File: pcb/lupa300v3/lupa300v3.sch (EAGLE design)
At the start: 17 parts

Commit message: more work
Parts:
- added C1, C2, C3, C4, C5, C6: .1uF, rcl:C-USC0603K
- added JP1, JP2: (no value), pinhead:PINHD-2X8
- added R12, R13, R14, R15, R16, R17, R18, R23: (no value), rcl:R-US_R0603
- added R19: 500k, rcl:R-US_R0603
- added R20: 1.5M, rcl:R-US_R0603
- added R21: 42k, rcl:R-US_R0603
- added R22: 110k, rcl:R-US_R0603
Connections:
- new net ADC_BIAS: C1.1, R12.1, U$1.ADC_BIAS
- new net BIAS1: C2.1, R19.1, U$1.BIAS1
- new net BIAS2: C3.1, R20.1, U$1.BIAS2
- new net BIAS3: C4.1, R21.1, U$1.BIAS3
- new net BIAS4: C5.1, R22.1, U$1.BIAS4
- new net N$27: U$1.VRESET_3
- new net N$28: U$1.VRESET_2
- new net N$29: U$2.GND
- new net N$30: U$2.VIN
- new net N$58: JP1.1
- new net N$59: JP1.3
- new net N$60: JP1.5
- new net N$61: JP1.7
- new net N$62: JP1.9
- new net N$63: JP1.11
- new net N$64: JP1.13
- new net N$65: JP1.15
- new net N$66: JP1.2
- new net N$67: JP1.4
- new net N$68: JP1.6
- new net N$69: JP1.8
- new net N$70: JP1.10
- new net N$71: JP1.12
- new net N$72: JP1.14
- new net N$73: JP1.16
- new net N$74: JP2.1
- new net N$75: JP2.3
- new net N$76: JP2.5
- new net N$77: JP2.7
- new net N$78: JP2.9
- new net N$79: JP2.11
- new net N$80: JP2.13
- new net N$81: JP2.15
- new net N$82: JP2.2
- new net N$83: JP2.4
- new net N$84: JP2.6
- new net N$85: JP2.8
- new net N$86: JP2.10
- new net N$87: JP2.12
- new net N$88: JP2.14
- new net N$89: JP2.16
- new net PRE_BIAS: C6.1, R23.1, U$1.PRECHARGE_BIAS
- net GNDA: now also C2.2, C3.2, C4.2, C5.2
- net GNDADC: now also C1.2
- net GND_PIX: now also C6.2
- net INT1: now also R18.1
- net INT2: now also R17.1
- net N$21: now also R13.1
- net N$23: now also R14.1
- net N$24: now also R15.1
- net N$25: now also R16.1
- net VADC: now also R12.2
- net VDDA: now also R19.2, R20.2, R21.2, R22.2
- net VPIX: now also R23.2

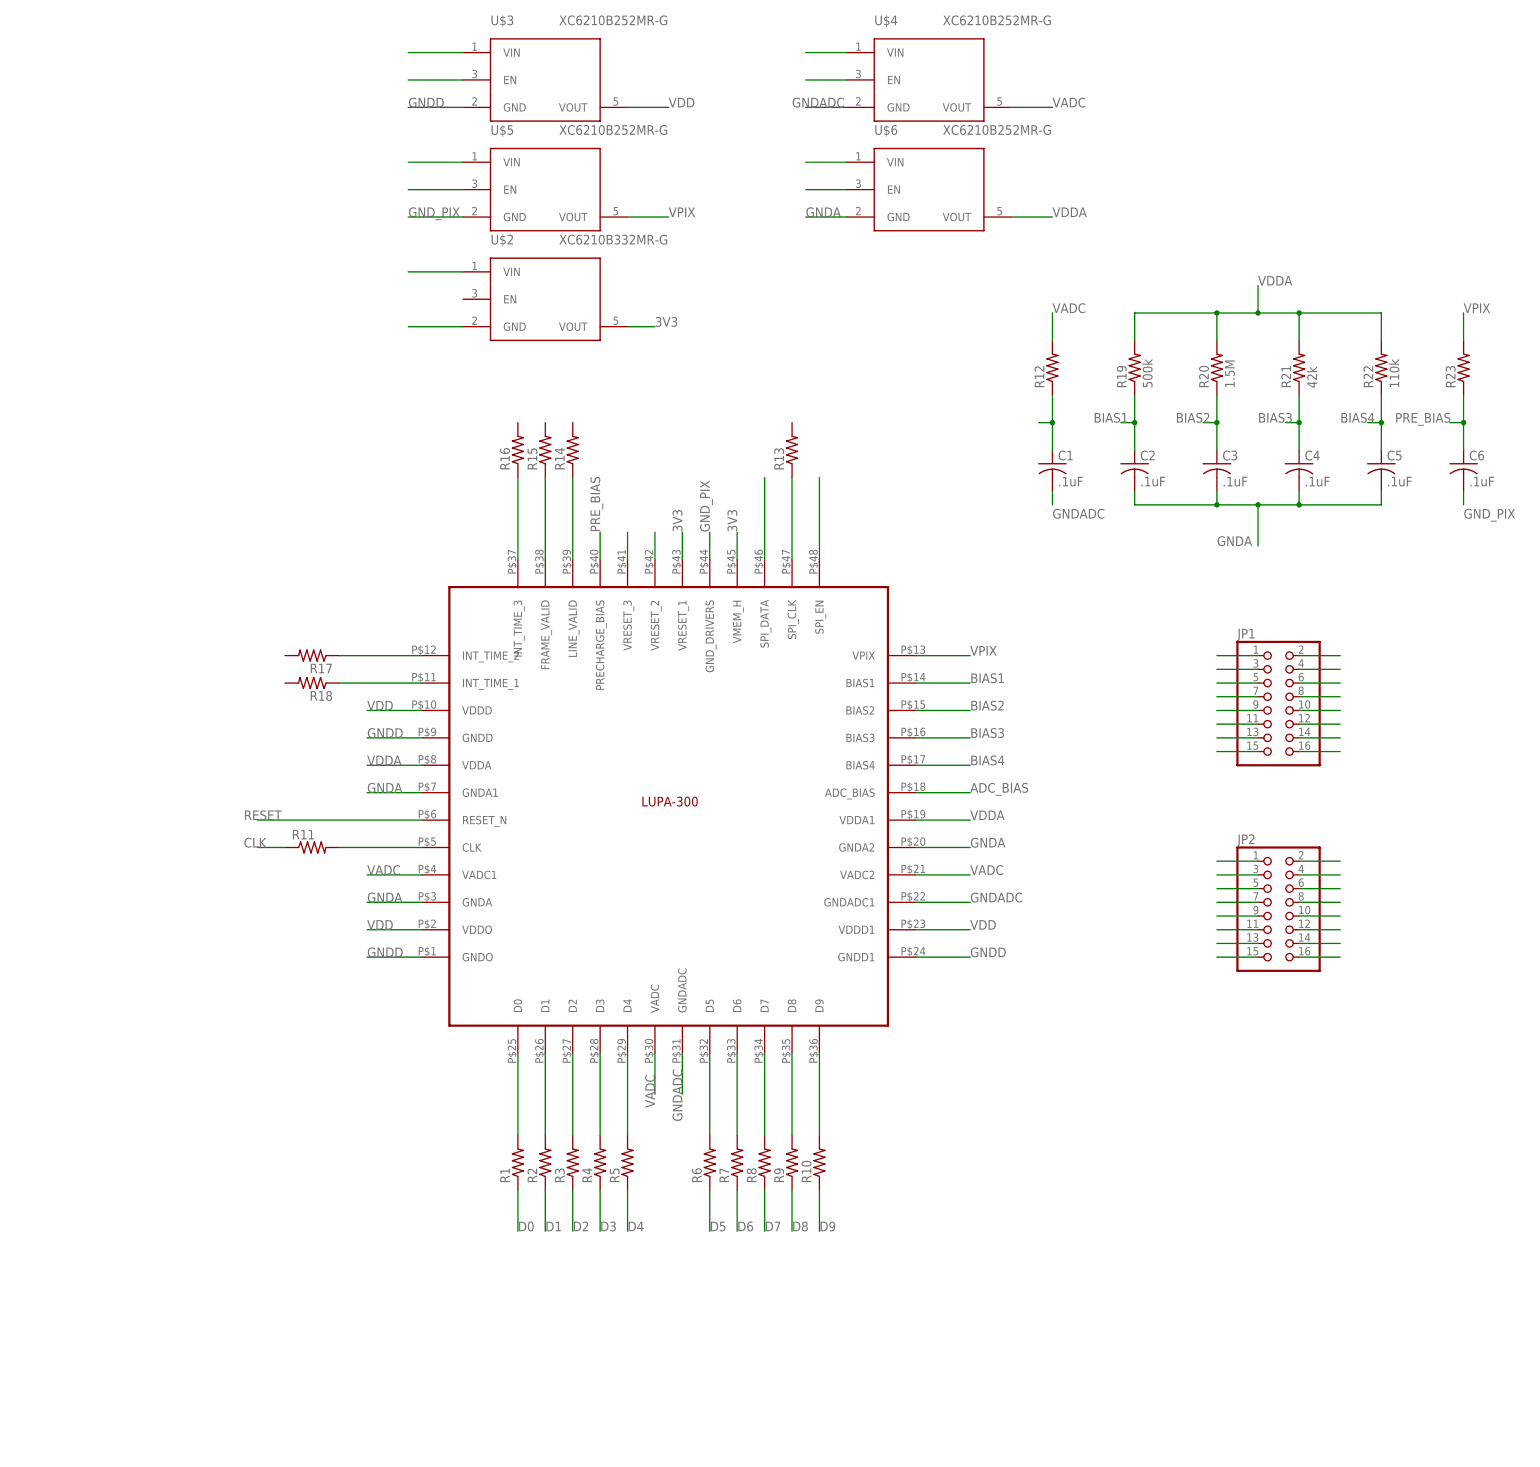
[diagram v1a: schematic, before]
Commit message: added adc output buffer
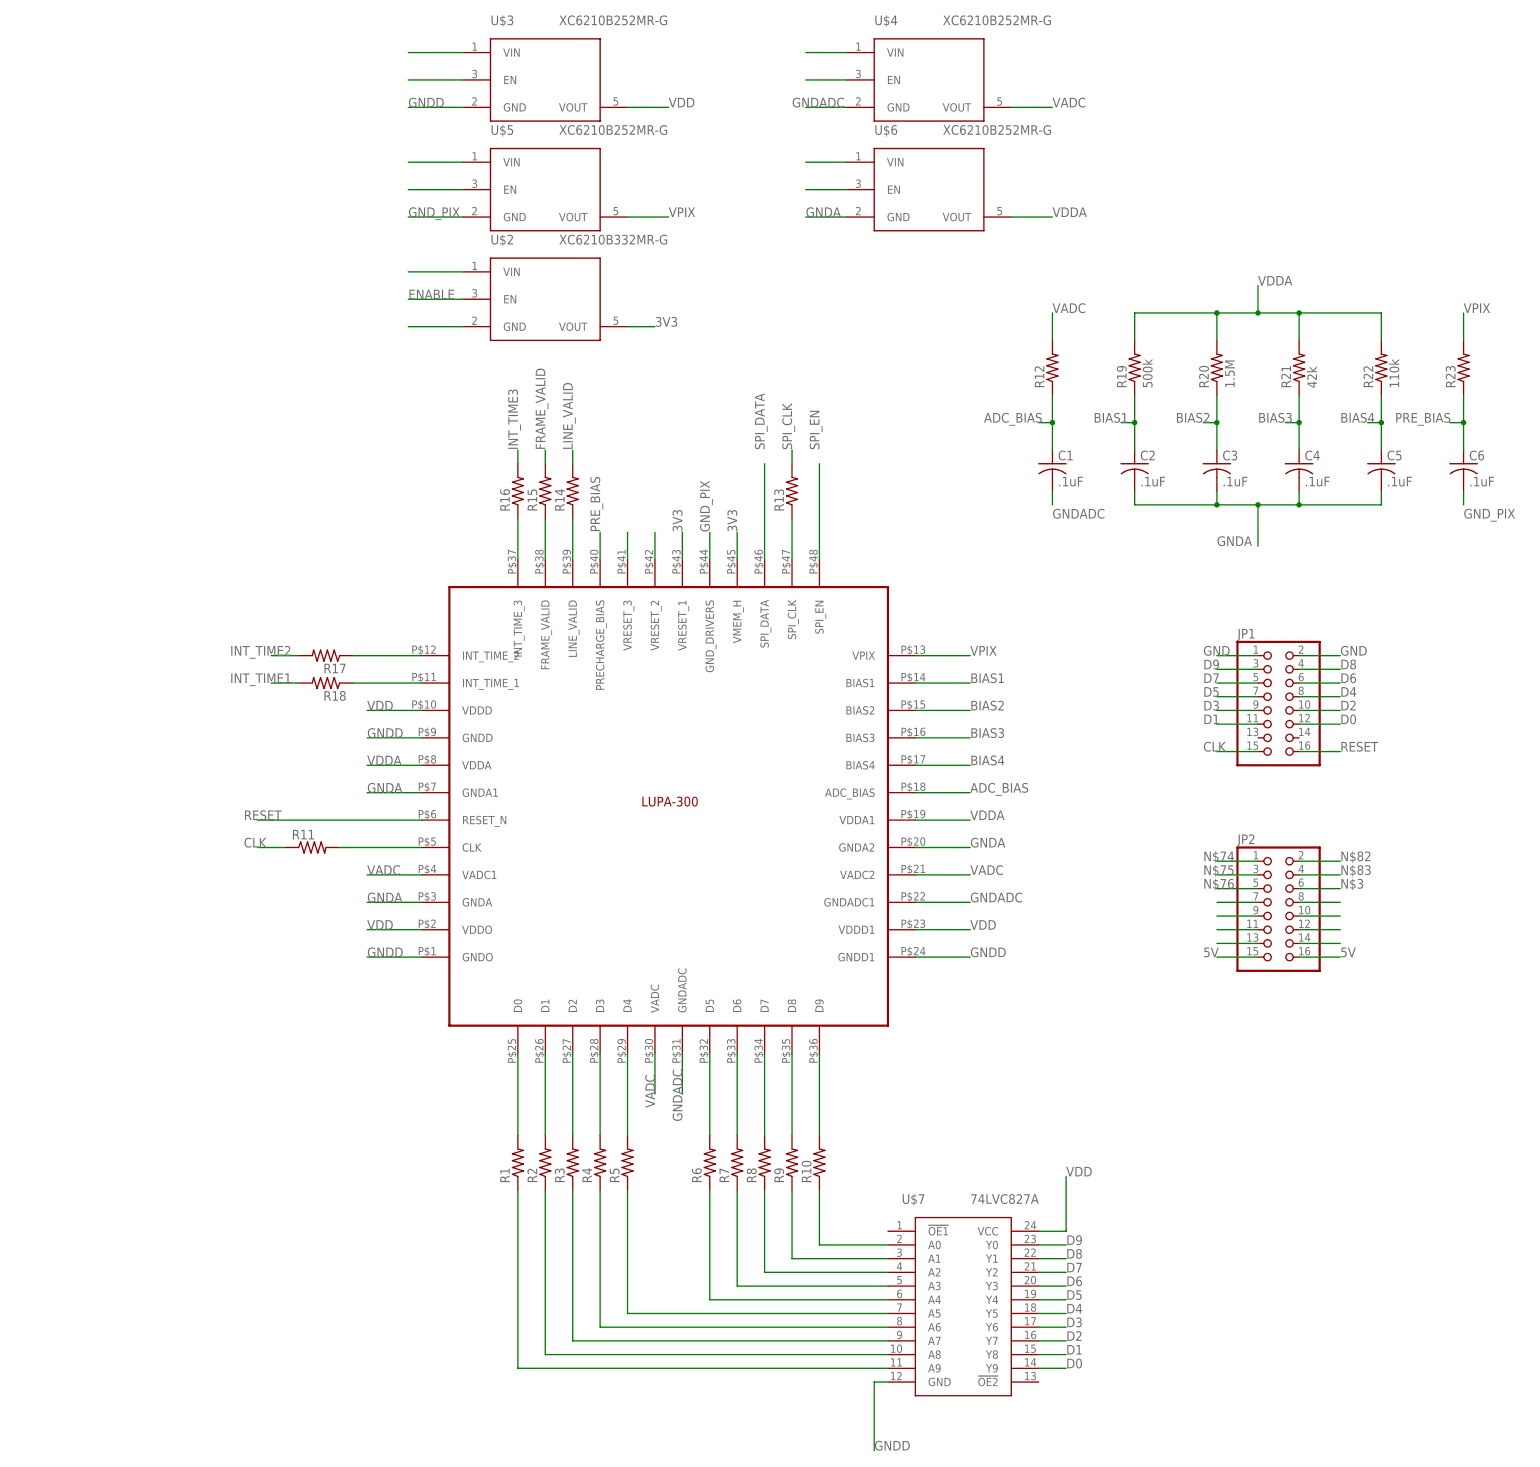
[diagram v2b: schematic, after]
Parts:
- added U$7: 74LVC827A, lupa300-components:74LVC827A
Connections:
- net N$20 renamed SPI_EN
- net N$22 renamed SPI_DATA
- removed net N$10 (its old number): U$4.EN
- removed net N$11 (its old number): U$6.VIN
- removed net N$12 (its old number): U$6.EN
- removed net N$3 (its old number): U$5.EN
- removed net N$30: U$2.VIN
- removed net N$4 (its old number): U$5.VIN
- removed net N$58: JP1.1
- removed net N$59: JP1.3
- removed net N$6 (its old number): U$3.EN
- removed net N$60: JP1.5
- removed net N$61: JP1.7
- removed net N$62: JP1.9
- removed net N$63: JP1.11
- removed net N$64: JP1.13
- removed net N$65: JP1.15
- removed net N$66: JP1.2
- removed net N$67: JP1.4
- removed net N$68: JP1.6
- removed net N$69: JP1.8
- removed net N$7 (its old number): U$3.VIN
- removed net N$70: JP1.10
- removed net N$71: JP1.12
- removed net N$72: JP1.14
- removed net N$73: JP1.16
- removed net N$8 (its old number): U$4.VIN
- removed net N$81: JP2.15
- removed net N$89: JP2.16
- new net 5V: JP2.15, JP2.16, U$2.VIN, U$3.VIN, U$4.VIN, U$5.VIN, U$6.VIN
- new net ENABLE: U$2.EN, U$3.EN, U$4.EN, U$5.EN, U$6.EN
- new net FRAME_VALID: R15.2
- new net GND: JP1.1, JP1.2
- new net INT_TIME1: R18.2
- new net INT_TIME2: R17.2
- new net INT_TIME3: R16.2
- new net LINE_VALID: R14.2
- new net N$26: R10.1, U$7.A0
- new net N$31: R9.1, U$7.A1
- new net N$32: R8.1, U$7.A2
- new net N$33: R7.1, U$7.A3
- new net N$34: R6.1, U$7.A4
- new net N$35: R5.1, U$7.A5
- new net N$36: R4.1, U$7.A6
- new net N$37: R3.1, U$7.A7
- new net N$38: R2.1, U$7.A8
- new net N$39: R1.1, U$7.A9
- new net SPI_CLK: R13.2
- net CLK: now also JP1.15
- net D0: now also JP1.12, U$7.Y9; no longer R1.1
- net D1: now also JP1.11, U$7.Y8; no longer R2.1
- net D2: now also JP1.10, U$7.Y7; no longer R3.1
- net D3: now also JP1.9, U$7.Y6; no longer R4.1
- net D4: now also JP1.8, U$7.Y5; no longer R5.1
- net D5: now also JP1.7, U$7.Y4; no longer R6.1
- net D6: now also JP1.6, U$7.Y3; no longer R7.1
- net D7: now also JP1.5, U$7.Y2; no longer R8.1
- net D8: now also JP1.4, U$7.Y1; no longer R9.1
- net D9: now also JP1.3, U$7.Y0; no longer R10.1
- net GNDD: now also U$7.GND
- net RESET: now also JP1.16
- net VDD: now also U$7.VCC
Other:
- moved on the sheet: R13, R14, R15, R16, R17, R18
